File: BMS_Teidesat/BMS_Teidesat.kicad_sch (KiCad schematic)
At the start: 73 parts, among them J1 Battery, U1 MCP1407-E_SN, U10 IPT004N03L, U11 IPT004N03L, U12 IPT004N03L, U13 MCP1407-E_SN, U14 AD7091R-8BCPZ-RL7, U15 AD8605ACBZ-REEL7, U2 AD8606ARMZ-REEL, U3 AD8605ACBZ-REEL7, U4 IPT004N03L, U5 IPT004N03L, U6 IPT004N03L, U7 ADA4940-1ACPZ-R7, U8 ACS37002LMCATR-050B5, U9 TMS5703137DPGEQQ1

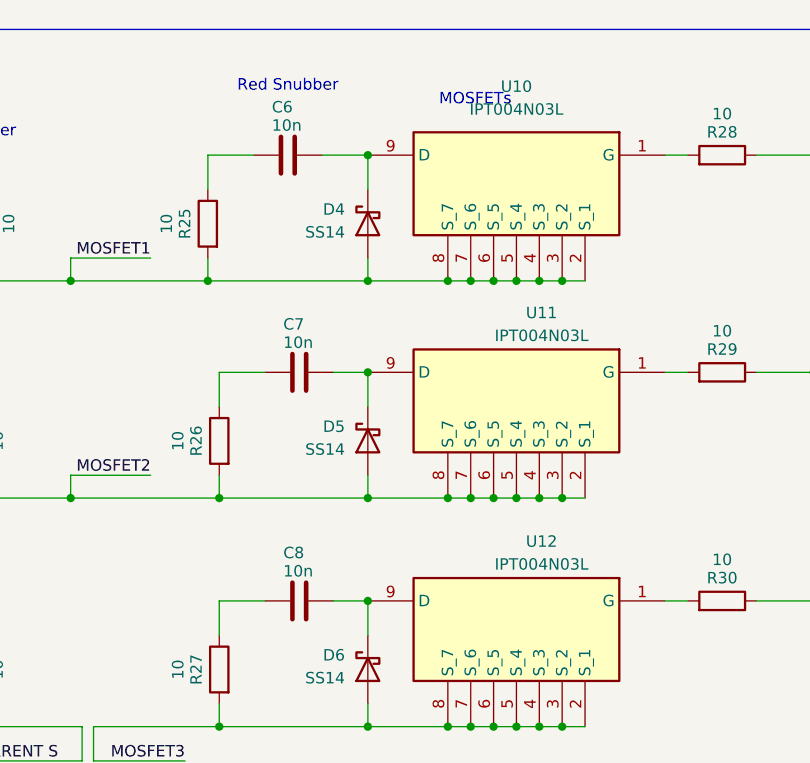
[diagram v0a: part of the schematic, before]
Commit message: Salida EPS añadida
Co-Authored-By: hugohdezmo <238262256+hugohdezmo@users.noreply.github.com>
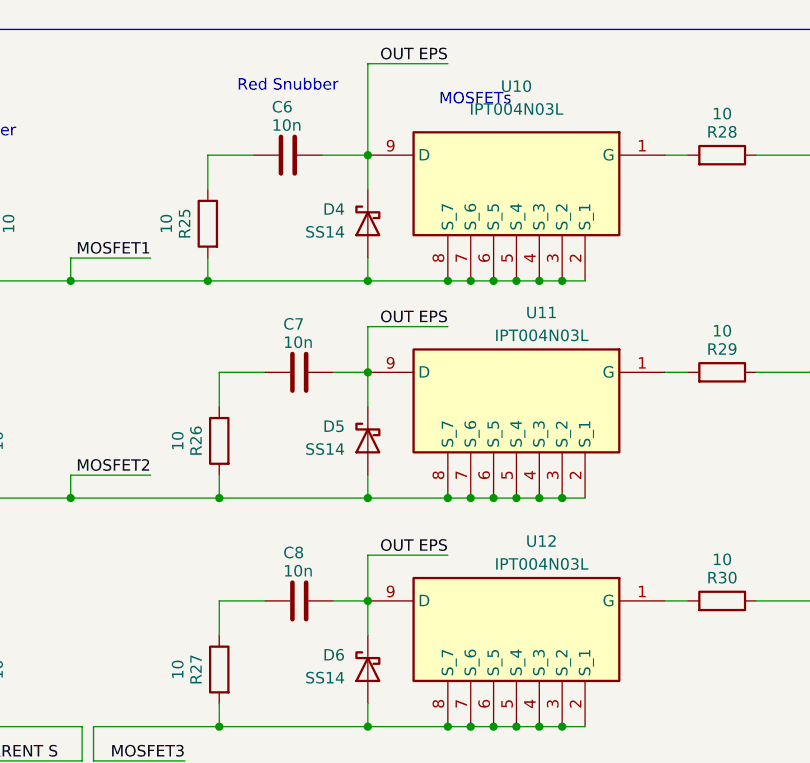
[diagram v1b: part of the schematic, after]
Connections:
- net OUT EPS: now reaches C8.1, D6.1 (K), U12.9 (D)
- net OUT EPS: now also C6.1, C7.1, D4.1 (K), D5.1 (K), U10.9 (D), U11.9 (D)
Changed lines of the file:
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@@
+	(wire
+		(pts
+			(xy 187.96 72.39) (xy 196.85 72.39)
+		)
+		(stroke
+			(width 0)
+			(type default)
+		)
+	)
+	(wire
+		(pts
+			(xy 187.96 72.39) (xy 187.96 77.47)
+		)
+		(stroke
+			(width 0)
+			(type default)
+		)
+	)
 	(wire
 		(pts
@@
 	(wire
 		(pts
+			(xy 187.96 17.78) (xy 196.85 17.78)
+		)
+		(stroke
+			(width 0)
+			(type default)
+		)
+	)
+	(wire
+		(pts
+			(xy 187.96 17.78) (xy 187.96 27.94)
+		)
+		(stroke
+			(width 0)
+			(type default)
+		)
+	)
+	(wire
+		(pts
+			(xy 187.96 46.99) (xy 187.96 52.07)
+		)
+		(stroke
+			(width 0)
+			(type default)
+		)
+	)
+	(wire
+		(pts
 			(xy 77.47 120.65) (xy 95.25 120.65)
 		)
@@
 		(pts
 			(xy 344.17 196.85) (xy 353.06 196.85)
+		)
+		(stroke
+			(width 0)
+			(type default)
+		)
+	)
+	(wire
+		(pts
+			(xy 187.96 46.99) (xy 196.85 46.99)
 		)
 		(stroke
@@
 		)
 	)
+	(label "OUT EPS"
+		(at 196.85 17.78 180)
+		(effects
+			(font
+				(size 1.27 1.27)
+			)
+			(justify right bottom)
+		)
+	)
 	(label "REFOUT"
 		(at 330.2 219.71 0)
@@
 		)
 	)
+	(label "OUT EPS"
+		(at 196.85 72.39 180)
+		(effects
+			(font
+				(size 1.27 1.27)
+			)
+			(justify right bottom)
+		)
+	)
 	(label "MOSFET2"
 		(at 163.83 63.5 180)
 		(effects
 			(font
+				(size 1.27 1.27)
+			)
+			(justify right bottom)
+		)
+	)
+	(label "OUT EPS"
+		(at 196.85 46.99 180)
+		(effects
+			(font

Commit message: Ajustes PCB
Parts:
- D1, D2, D3, D4, D5, D6: footprint Huellas BMS:DIOM6859X262N -> Huellas BMS:DIOM8059X256N
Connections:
- net +3V3: now also H1.47 (Pin_47), H1.48 (Pin_48), H1.49 (Pin_49), H1.50 (Pin_50), H1.51 (Pin_51), H1.52 (Pin_52), H2.18 (Pin_18), H2.19 (Pin_19), H2.20 (Pin_20)
- no-connect marks 254 -> 245
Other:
- moved on the sheet: H1, H2

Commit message: Circuito de potencia PCB
Se ha elaborado el circuito de potencia de en la PCB incorporando los 3 mosfets y los 3 sensores de temperatura.

Co-Authored-By: Angel-Castro-Vega <236372966+Angel-Castro-Vega@users.noreply.github.com>
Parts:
- added C14, C15: 1n, Capacitor_SMD:C_0805_2012Metric, symbol Device:C
- added R32, R39: 50,5K, Resistor_SMD:R_0201_0603Metric, symbol Device:R
- added R33, R40: 50,5k, Resistor_SMD:R_0201_0603Metric, symbol Device:R
- added R34, R35, R41, R42: 80,6K, Resistor_SMD:R_0201_0603Metric, symbol Device:R
- added R36, R43: 40,2K, Resistor_SMD:R_0201_0603Metric, symbol Device:R
- added R37, R44: 10K, Resistor_SMD:R_0201_0603Metric, symbol Device:R
- added R38, R45: 100, Resistor_SMD:R_0201_0603Metric, symbol Device:R
- added U16, U18: AD8606ARMZ-REEL, Huellas BMS:SOP65P490X110-8N, symbol AD8606ARMZ-REEL:AD8606ARMZ-REEL
- added U17, U19: ACS37002LMCATR-050B5, Huellas BMS:ACS37002LMCA050U5, symbol ACS37002LMCATR-050B5:ACS37002LMCATR-050B5
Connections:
- net +5V: now also U16.8 (V+), U17.10 (VCC), U18.8 (V+), U19.10 (VCC)
- net GND: now also C14.1, C15.1, R33.1, R37.2, R40.1, R44.2, U16.4 (V-), U17.15 (GND), U18.4 (V-), U19.15 (GND)
- net MOSFET1: now also U8.5 (IP-_1), U8.6 (IP-_2), U8.7 (IP-_3), U8.8 (IP-_4); no longer D1.2 (A), R23.2, U4.2 (S_1), U4.3 (S_2), U4.4 (S_3), U4.5 (S_4), U4.6 (S_5), U4.7 (S_6), U4.8 (S_7)
- net MOSFET2: now also U17.5 (IP-_1), U17.6 (IP-_2), U17.7 (IP-_3), U17.8 (IP-_4); no longer D2.2 (A), R21.2, U5.2 (S_1), U5.3 (S_2), U5.4 (S_3), U5.5 (S_4), U5.6 (S_5), U5.7 (S_6), U5.8 (S_7)
- net MOSFET3: now also U19.5 (IP-_1), U19.6 (IP-_2), U19.7 (IP-_3), U19.8 (IP-_4); no longer U8.5 (IP-_1), U8.6 (IP-_2), U8.7 (IP-_3), U8.8 (IP-_4)
- net REFOUT: now also R36.1, R43.1
- net +HALL3: now reaches U14.12 (VIN5)
- net +HALL3: now also R39.2, U18.7 (OUT_B)
- net +HALL2: now reaches U14.9 (VIN4)
- net +HALL2: now also R32.2, U16.7 (OUT_B)
- net +HALL renamed +HALL1
- net CURRENT S renamed CURRENT_3
- net CURRENT_3: now also U19.1 (IP+_1), U19.2 (IP+_2), U19.3 (IP+_3), U19.4 (IP+_4); no longer U8.1 (IP+_1), U8.2 (IP+_2), U8.3 (IP+_3), U8.4 (IP+_4)
- new net: C14.2, R35.1, R38.2
- new net: R33.2, R35.2, U16.5 (+IN_B)
- new net: R34.1, U16.1 (OUT_A), U16.2 (-IN_A)
- new net: R36.2, R37.1, U16.3 (+IN_A)
- new net: R32.1, R34.2, U16.6 (-IN_B)
- new net: R45.1, U19.12 (VIOUT)
- new net: C15.2, R42.1, R45.2
- new net: R41.1, U18.1 (OUT_A), U18.2 (-IN_A)
- new net: R39.1, R41.2, U18.6 (-IN_B)
- new net: R43.2, R44.1, U18.3 (+IN_A)
- new net: R38.1, U17.12 (VIOUT)
- new net: R40.2, R42.2, U18.5 (+IN_B)
- new net CURRENT_1: D1.2 (A), R23.2, U4.2 (S_1), U4.3 (S_2), U4.4 (S_3), U4.5 (S_4), U4.6 (S_5), U4.7 (S_6), U4.8 (S_7), U8.1 (IP+_1), U8.2 (IP+_2), U8.3 (IP+_3), U8.4 (IP+_4)
- new net CURRENT_2: D2.2 (A), R21.2, U17.1 (IP+_1), U17.2 (IP+_2), U17.3 (IP+_3), U17.4 (IP+_4), U5.2 (S_1), U5.3 (S_2), U5.4 (S_3), U5.5 (S_4), U5.6 (S_5), U5.7 (S_6), U5.8 (S_7)
- no-connect marks 245 -> 253
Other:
- moved on the sheet: C1, J1, R1, R13, R14, R16, R17, R18, R19, R20, R24, R5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
